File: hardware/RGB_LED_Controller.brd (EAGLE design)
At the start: 70 x 43 mm, 18 parts, among them IC2 MEGA8-AI, J2 CON_HEADER_1X04, Q1 MOSFET-NCHANNELFDD8580, Q2 MOSFET-NCHANNELFDD8580, Q4 MOSFET-NCHANNELFDD8580

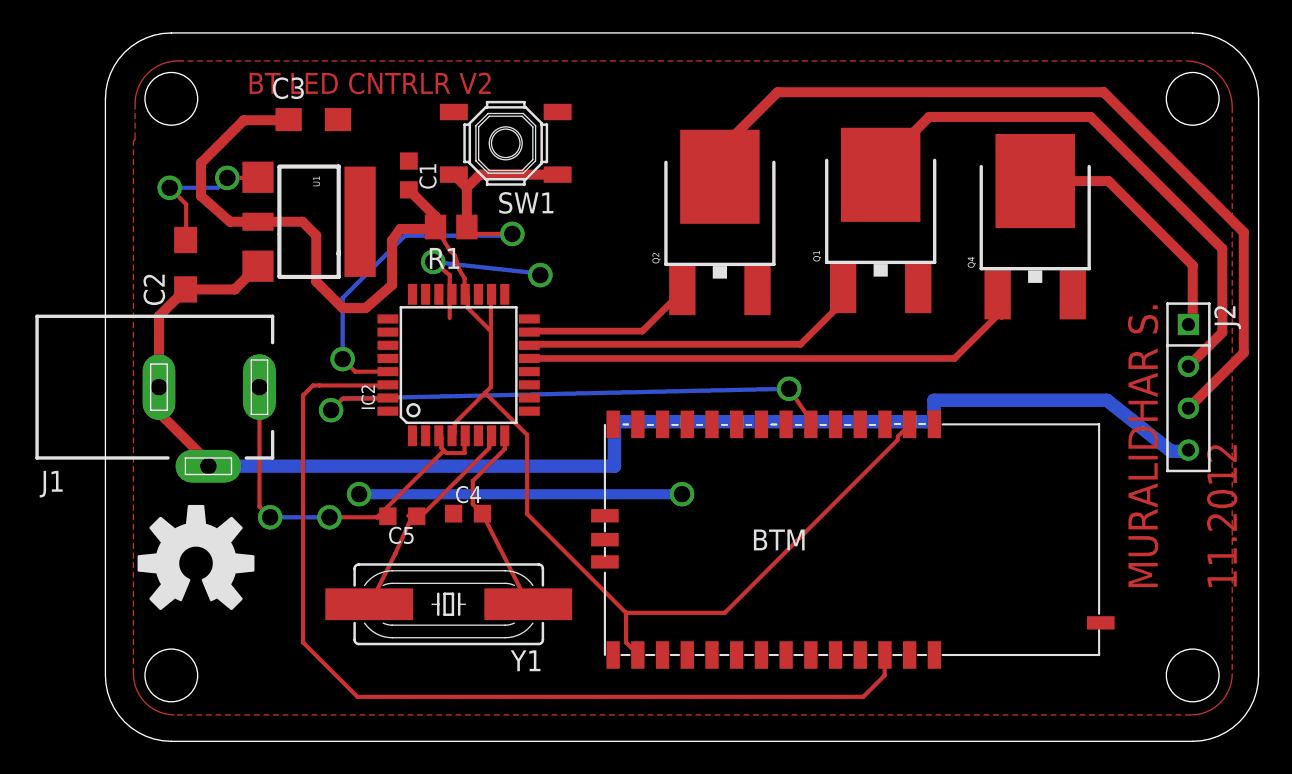
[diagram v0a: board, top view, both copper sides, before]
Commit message: schematic inconsistency with board issue resolved
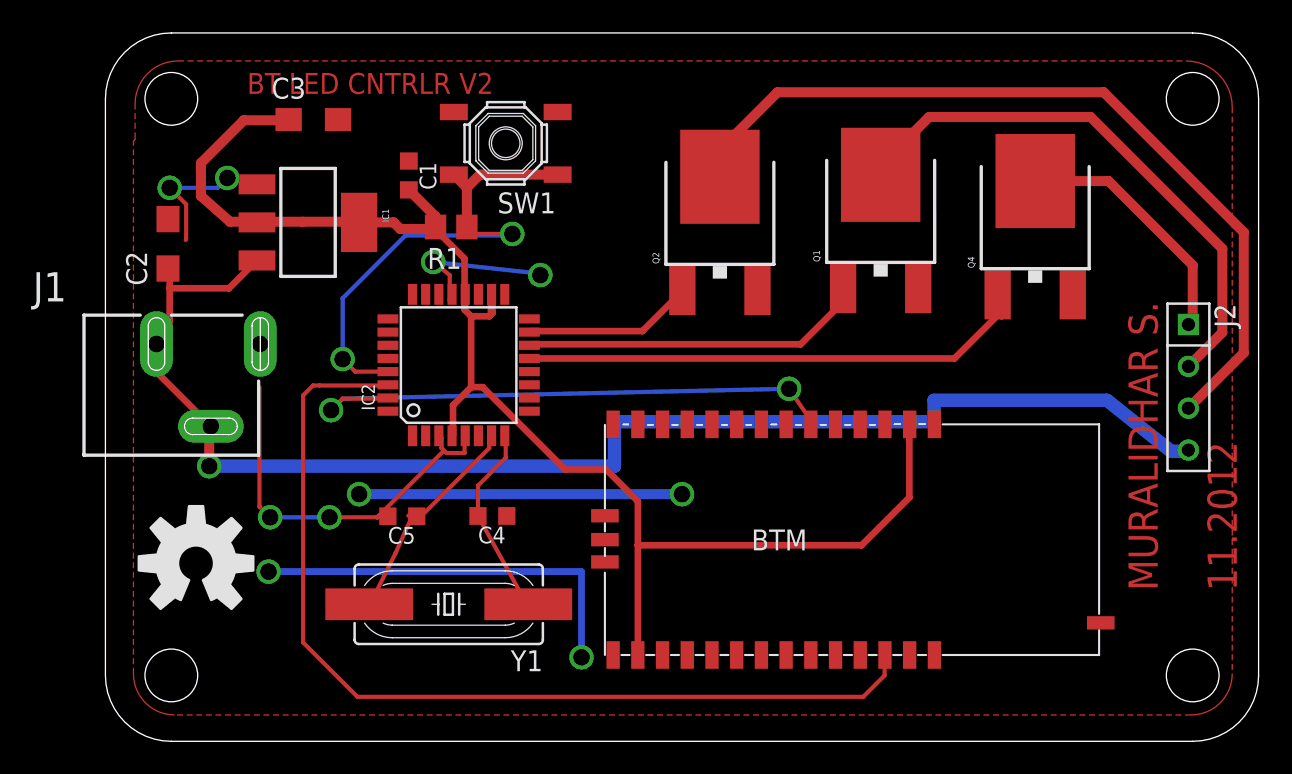
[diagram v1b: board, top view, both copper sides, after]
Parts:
- removed U1: (no value), microbuilder:SOT223-W
- added IC1: (no value), SparkFun:SOT223
- J1: value (none) -> POWER_JACKSLT; device con-jack:DCJ0303 -> SparkFun:POWER_JACK_SLOT
- moved J1 11.9 mm to (-4.40, 26.7)
- moved C2 1.66 mm to (3.80, 30.2)
- moved C4 1.49 mm to (23.5, 13.7), turned to 180 degrees
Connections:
- net +3V3: now also IC1.2, IC1.4; no longer U1.2
- net 12V: now also IC1.3, J1.GND@1, J1.GND@2; no longer J1.2, J1.3, U1.3
- net GND: now also IC1.1, J1.PWR; no longer J1.1, U1.1
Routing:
- net GND: track 65.8 -> 89.0 mm, vias 8 -> 10
- net 12V: track 82.4 -> 85.2 mm, vias 0 -> 1
- net +3V3: track 93.7 -> 92.3 mm

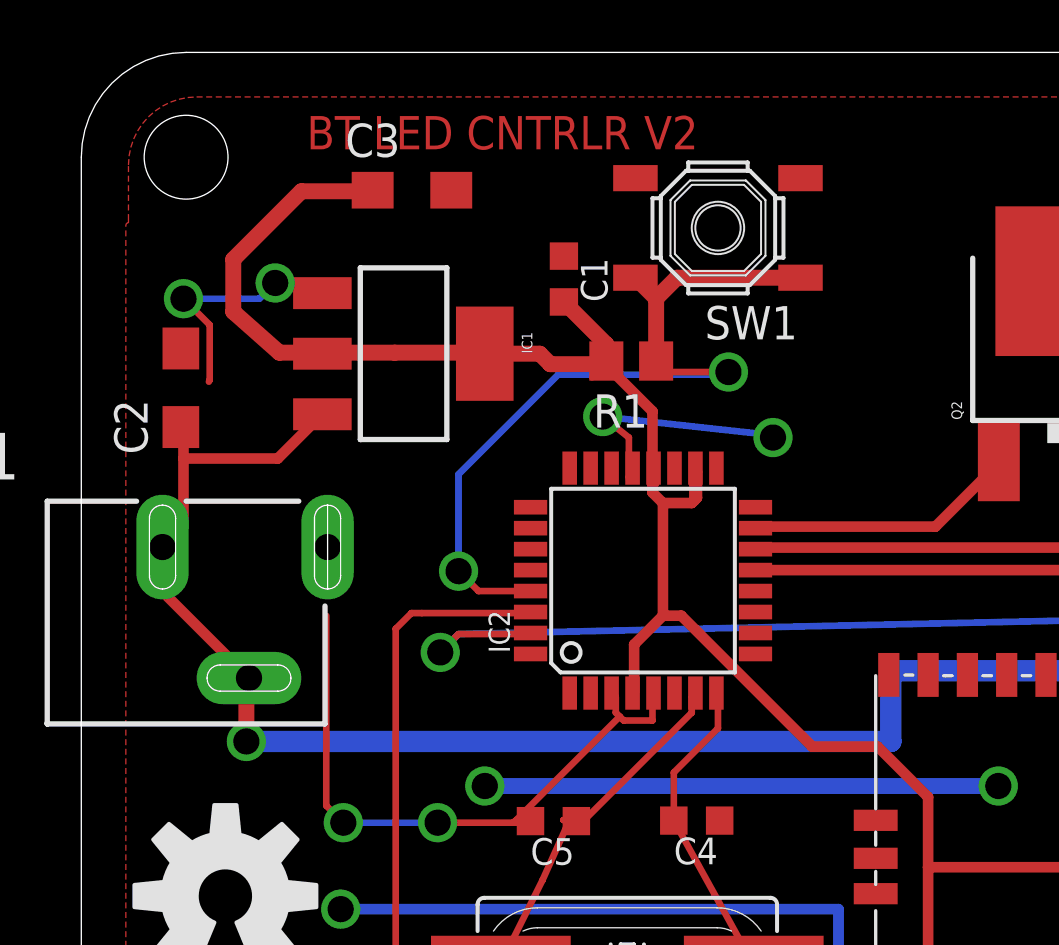
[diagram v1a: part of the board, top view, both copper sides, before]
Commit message: barrel jack was connected in reverse. corrected now.
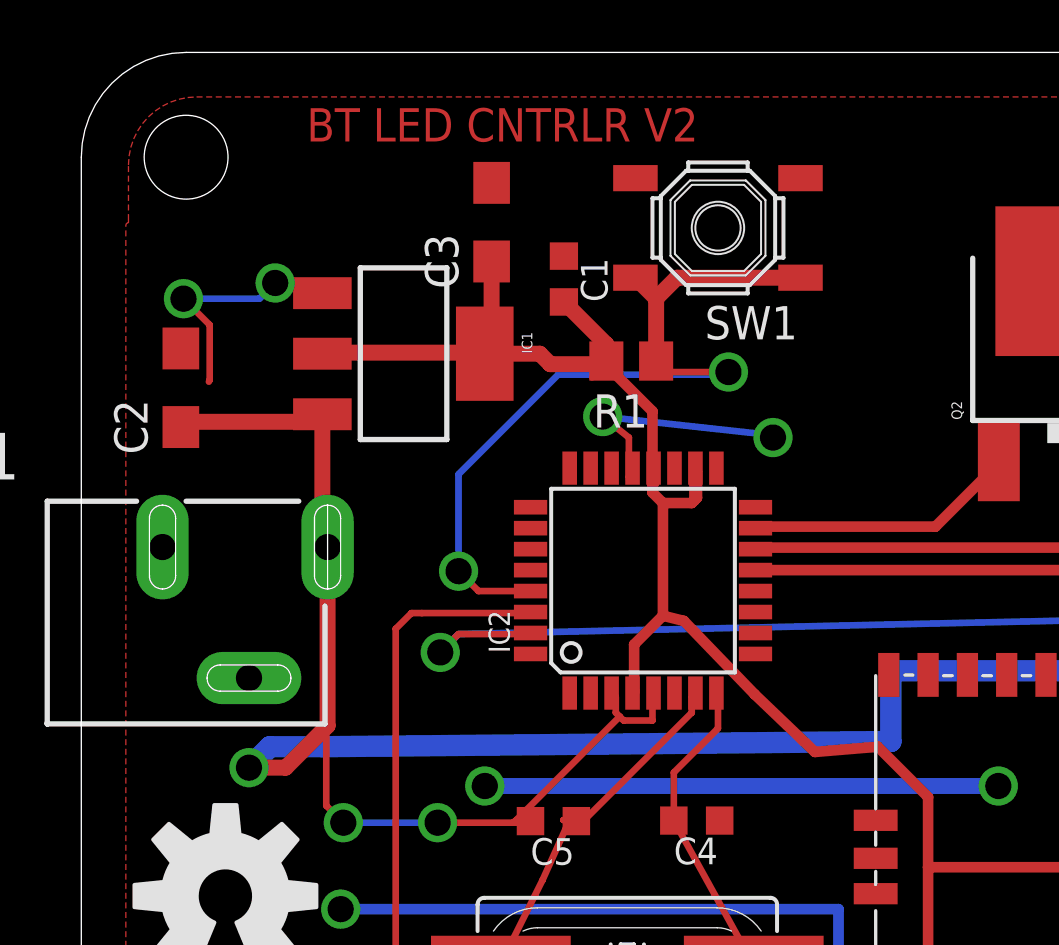
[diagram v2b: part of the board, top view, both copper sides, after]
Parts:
- moved C3 3.28 mm to (15.7, 36.5), turned to 90 degrees
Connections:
- net 12V: now also J1.PWR; no longer J1.GND@1, J1.GND@2
- net GND: now also J1.GND@1, J1.GND@2; no longer J1.PWR
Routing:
- net +3V3: track 92.3 -> 81.7 mm
- net 12V: track 85.2 -> 86.2 mm

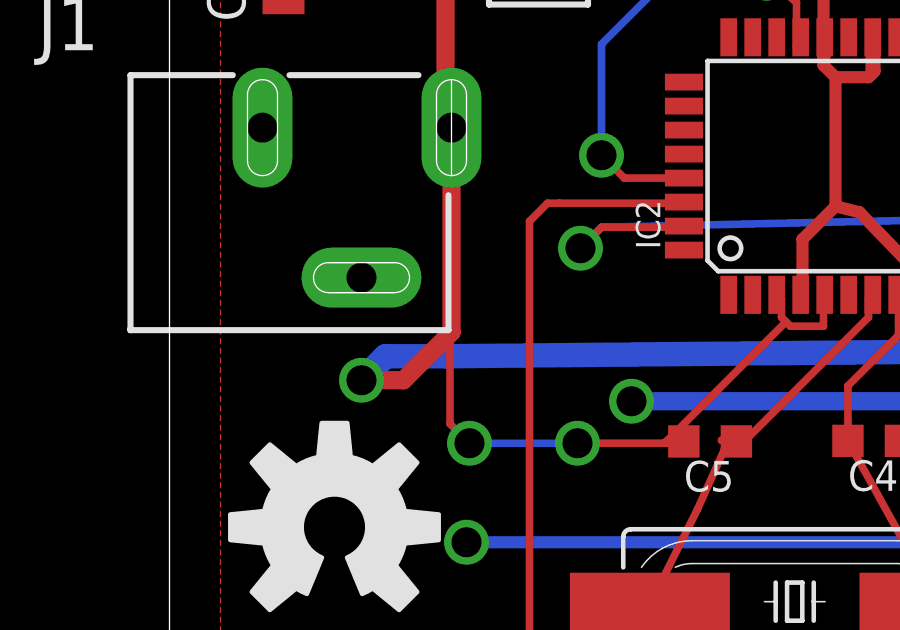
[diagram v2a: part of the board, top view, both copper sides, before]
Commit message: stray track removed
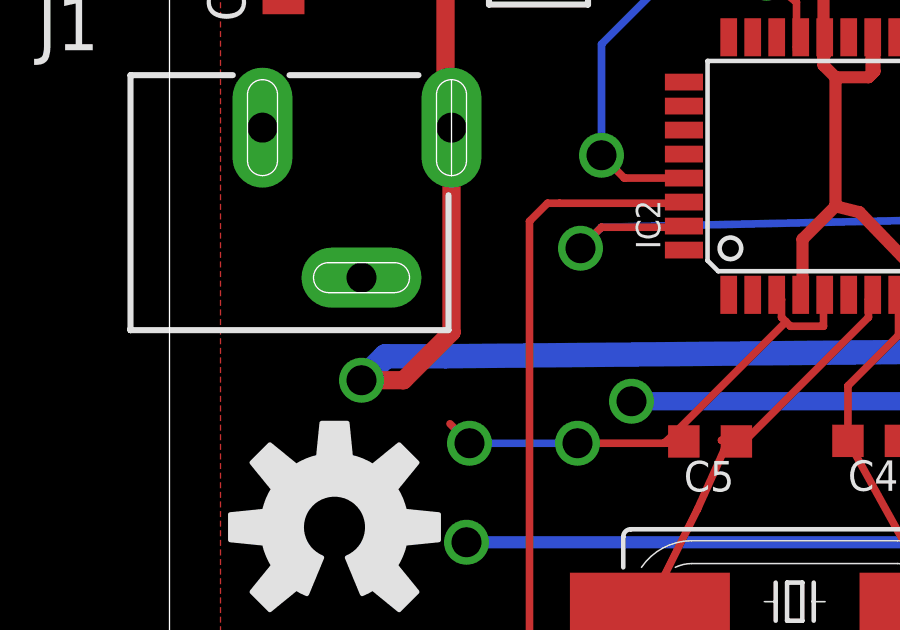
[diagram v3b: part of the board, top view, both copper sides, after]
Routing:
- net GND: track 89.0 -> 81.8 mm
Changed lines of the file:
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@@
 <?xml version="1.0" encoding="utf-8"?>
 <!DOCTYPE eagle SYSTEM "eagle.dtd">
-<eagle version="6.1">
+<eagle version="6.2">
 <drawing>
 <settings>
@@
 <board>
 <plain>
-<text x="7.66" y="40.7" size="1.778" layer="27">http://murlidharshenoy.wordpress.com/</text>
+<text x="14.16" y="40.7" size="1.778" layer="27">http://murlidharshenoy.wordpress.com/</text>
 <polygon width="0.4064" layer="41">
 <vertex x="52.2" y="19.4"/>
@@
 <wire x1="3.9" y1="33.6" x2="6.8" y2="33.6" width="0.254" layer="16"/>
 <wire x1="6.8" y1="33.6" x2="7.4" y2="34.2" width="0.254" layer="16"/>
-<wire x1="9.35" y1="21.5" x2="9.35" y2="14.25" width="0.254" layer="1"/>
 <wire x1="9.35" y1="14.25" x2="10" y2="13.6" width="0.254" layer="1"/>
 <via x="10" y="13.6" extent="1-16" drill="1"/>
@@
 <wire x1="15.66" y1="35.02" x2="15.66" y2="31.56" width="0.6096" layer="1"/>
 <wire x1="15.66" y1="31.56" x2="15.6" y2="31.5" width="0.6096" layer="1"/>
+<wire x1="23" y1="21.3" x2="25.7" y2="18.5" width="0.4064" layer="1"/>
+<wire x1="25.7" y1="18.5" x2="28" y2="16.3" width="0.4064" layer="1"/>
 <wire x1="9.2012" y1="31.5" x2="9.26" y2="31.54" width="0" layer="19" extent="1-1"/>
 <wire x1="9.2" y1="31.5" x2="9.2012" y2="31.5" width="0" layer="19" extent="1-1"/>
 <wire x1="20.04" y1="31.06" x2="20.1" y2="31.1" width="0" layer="19" extent="1-1"/>
-<wire x1="23" y1="21.3" x2="25.7" y2="18.5" width="0.4064" layer="1"/>
-<wire x1="25.7" y1="18.5" x2="28" y2="16.3" width="0.4064" layer="1"/>
 </signal>
 <signal name="N$6">

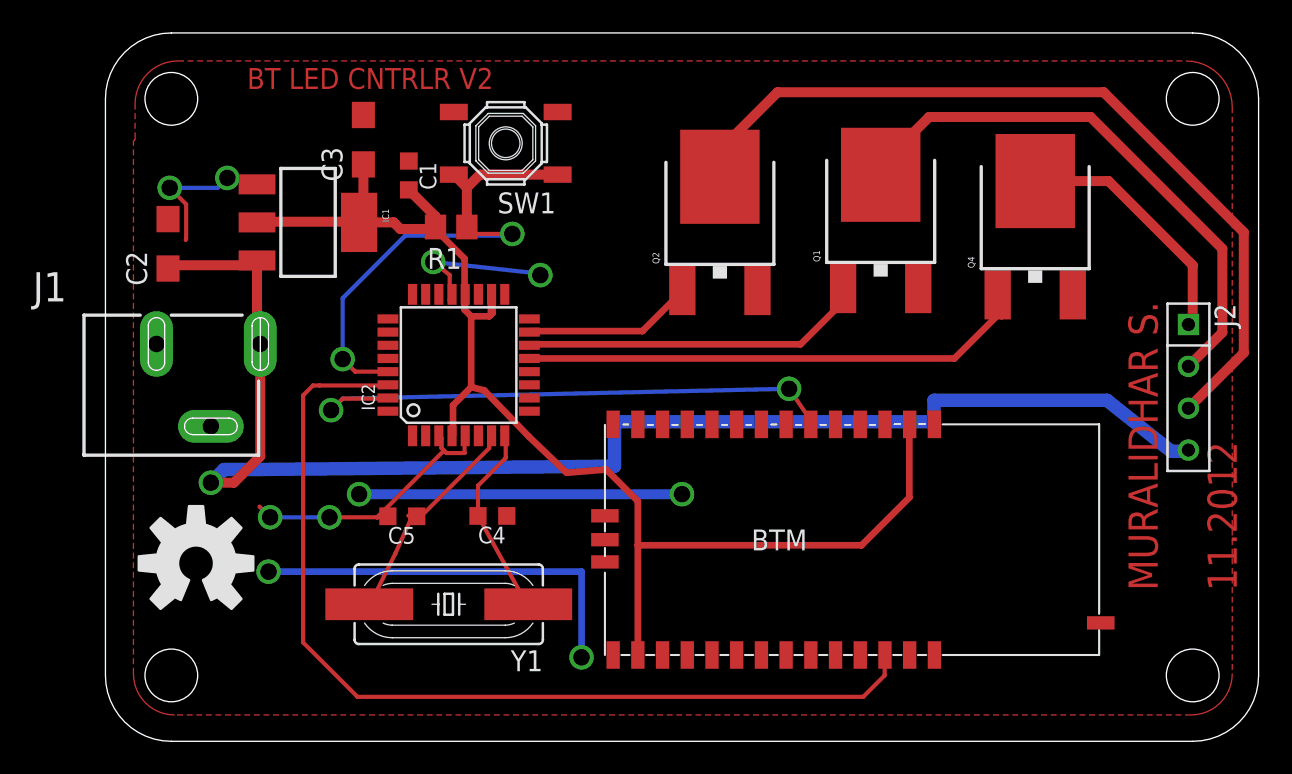
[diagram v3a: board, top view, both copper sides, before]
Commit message: Bluetooth module changed from aubtm-20 to more easily available HC-05. Footprints for through hole parts mirrored.
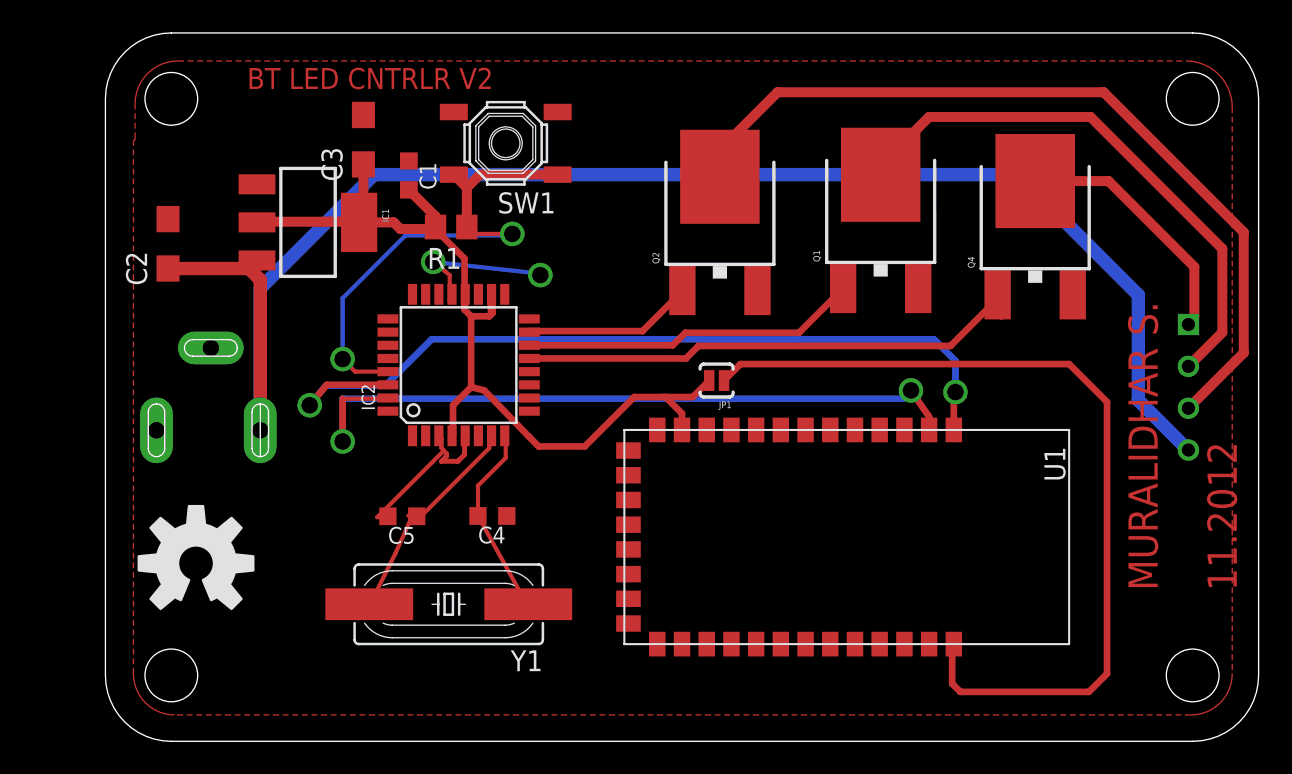
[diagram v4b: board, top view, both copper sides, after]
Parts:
- removed U$4: AUBTM-20, bluetooth:BT-MODULE
- added JP1: (no value), SparkFun:SJ_2S-NO
- added U1: HC_05, FarasbeeSerialPortBluetooth:BLUETOOTH_SMD
- moved J1 10.4 mm to (-4.40, 16.3), flipped to the bottom, turned to 90 degrees
- flipped J2 to the bottom
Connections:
- new net N$10: JP1.1, U1.34
- net +3V3: now also JP1.2, U1.12; no longer U$4.3V3, U$4.3V32
- net GND: now also U1.13, U1.21, U1.22; no longer U$4.GND, U$4.GND2, U$4.GND3, U$4.GND4, U$4.PIO5
- net RX: now also U1.2; no longer U$4.RXD
- net TX: now also U1.1; no longer U$4.TXD
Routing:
- net GND: track 81.8 -> 21.7 mm, vias 10 -> 2
- net N$10: track 0.00 -> 53.6 mm
- net +3V3: track 81.7 -> 57.1 mm
- net RX: track 34.5 -> 45.7 mm
- net 12V: track 86.2 -> 94.3 mm, vias 1 -> 0
- net TX: track 58.9 -> 51.2 mm, vias 0 -> 2

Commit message: rev 3 PCB. Printout taken
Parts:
- moved E$1 36.4 mm to (41.9, 12.3)
